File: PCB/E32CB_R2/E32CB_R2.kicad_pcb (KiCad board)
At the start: 2 copper layers, 111.3 x 90.9 mm, 89 parts, among them J1 GPIO_HEADER, J10 S, J11 Q4, J12 S, J13 Q3, J14 S, J15 Q8, J16 S, J17 Q7, J18 S, J19 Q6, J2 Power, J20 S, J21 Q5, J22 S, J3 USB_B, J4 USB +5V, J5 NEXTION, J6 I2C, J7 Q1, J8 S, J9 Q2, Q1 S8050, Q10 IRLR2905, Q2 S8050, Q3 IRLR2905, Q4 IRLR2905, Q5 IRLR2905, Q6 IRLR2905, Q7 IRLR2905, Q8 IRLR2905, Q9 IRLR2905, U1 ESP32-WROOM-32, X1 12MHz

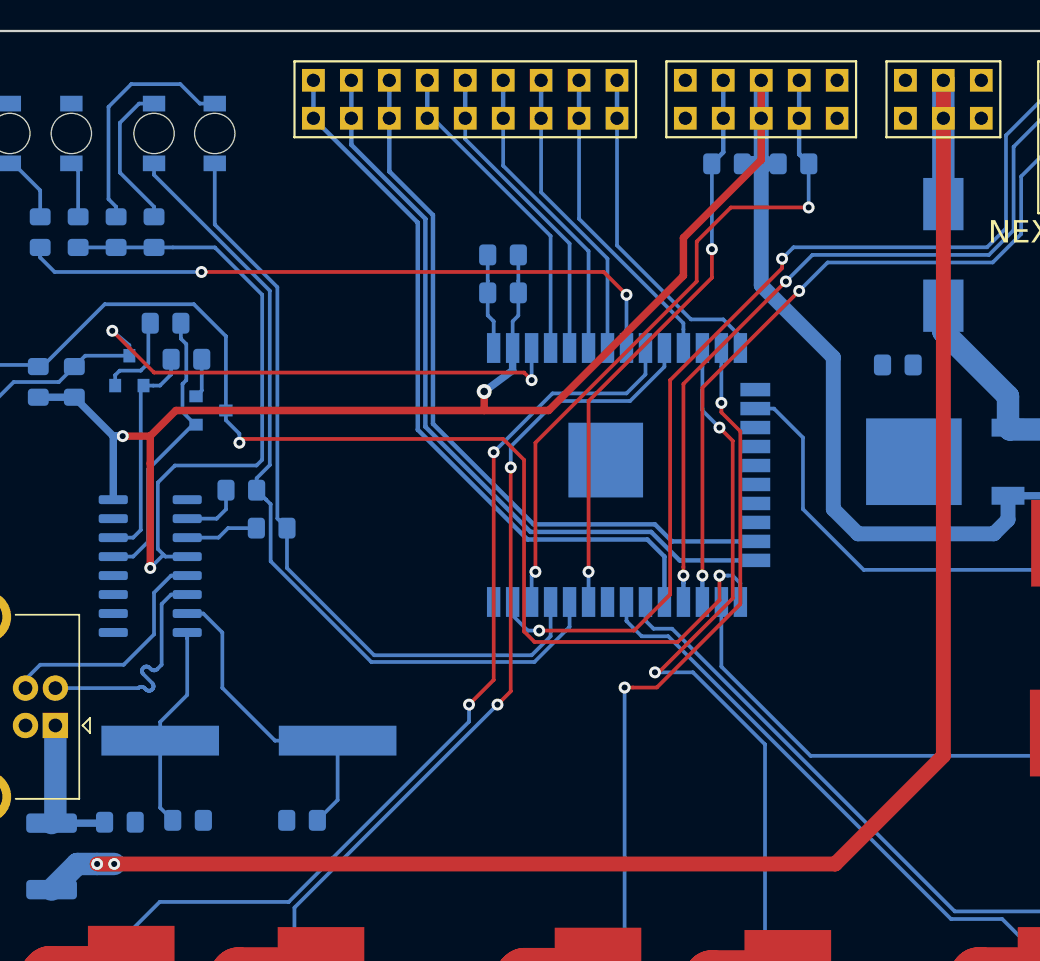
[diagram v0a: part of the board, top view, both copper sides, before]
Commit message: all conection finished
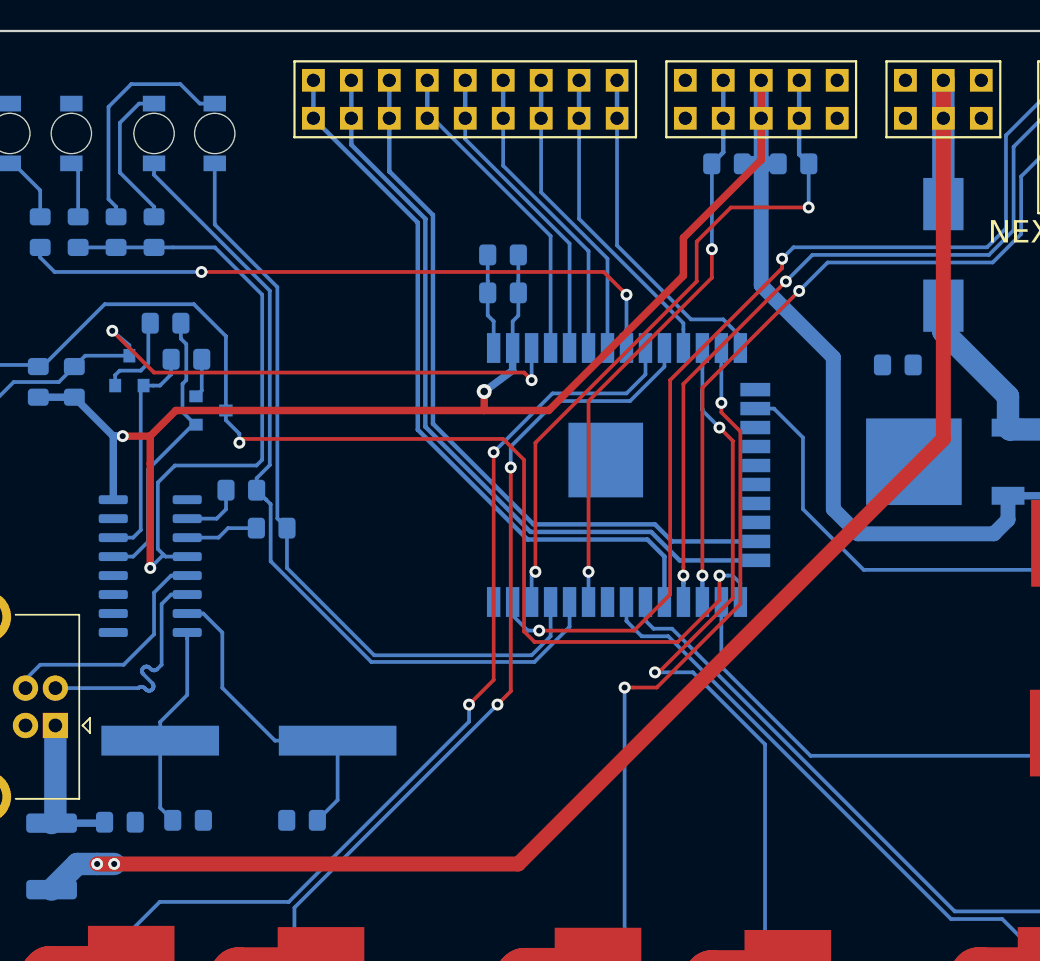
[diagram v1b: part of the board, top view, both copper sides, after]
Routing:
- net +5V: track 118.0 -> 105.6 mm
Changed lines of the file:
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@@
   (segment (start 115.062 101.727) (end 116.205 101.727) (width 1.5) (layer B.Cu) (net 83))
   (via (at 115.062 101.727) (size 0.8) (drill 0.4) (layers F.Cu B.Cu) (net 83))
-  (segment (start 115.062 101.727) (end 164.465 101.727) (width 1) (layer F.Cu) (net 83))
-  (segment (start 171.704 94.488) (end 171.704 49.276) (width 1) (layer F.Cu) (net 83))
-  (segment (start 164.465 101.727) (end 171.704 94.488) (width 1) (layer F.Cu) (net 83))
+  (segment (start 171.704 73.279) (end 171.704 49.276) (width 1) (layer F.Cu) (net 83))
+  (segment (start 115.062 101.727) (end 143.256 101.727) (width 1) (layer F.Cu) (net 83))
+  (segment (start 143.256 101.727) (end 171.704 73.279) (width 1) (layer F.Cu) (net 83))
   (segment (start 112.268 98.74) (end 112.014 98.994) (width 1.5) (layer B.Cu) (net 84))
   (segment (start 112.268 92.456) (end 112.268 98.74) (width 1.5) (layer B.Cu) (net 84))

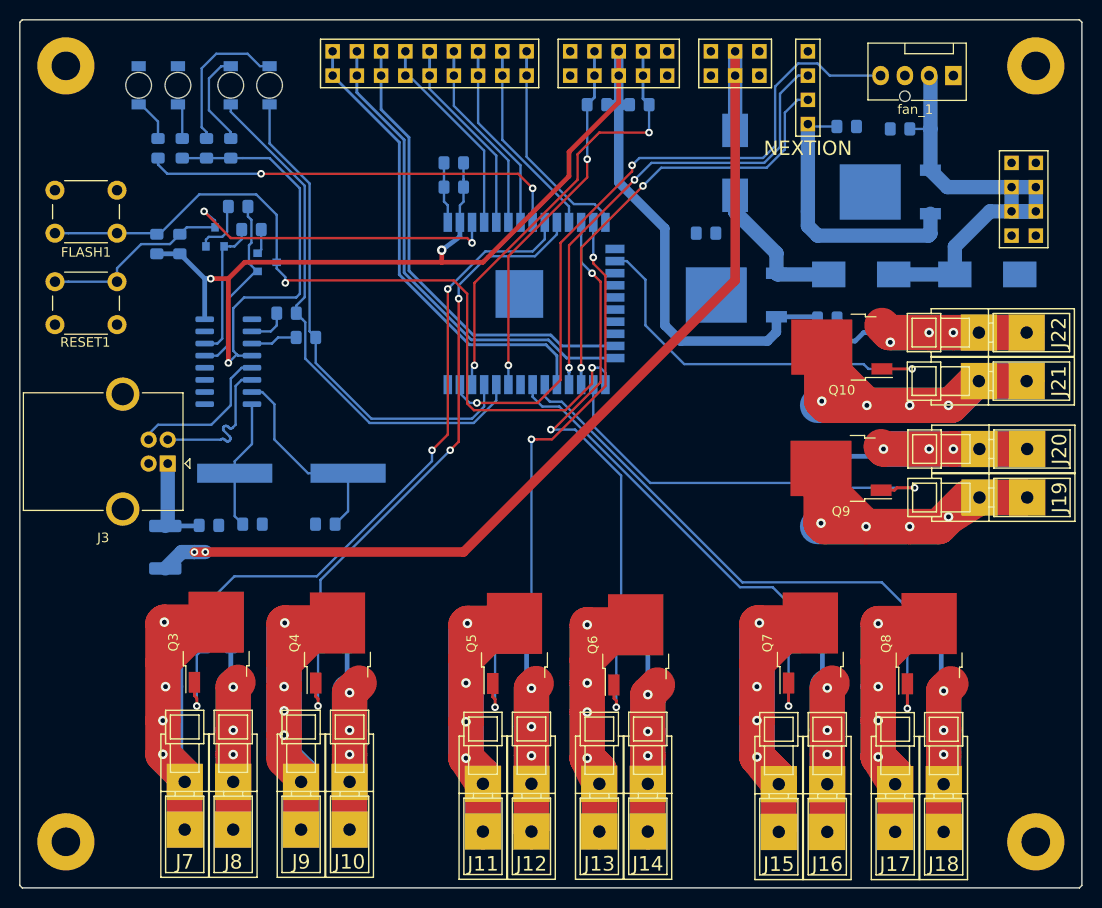
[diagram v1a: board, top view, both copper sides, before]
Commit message: filled zones
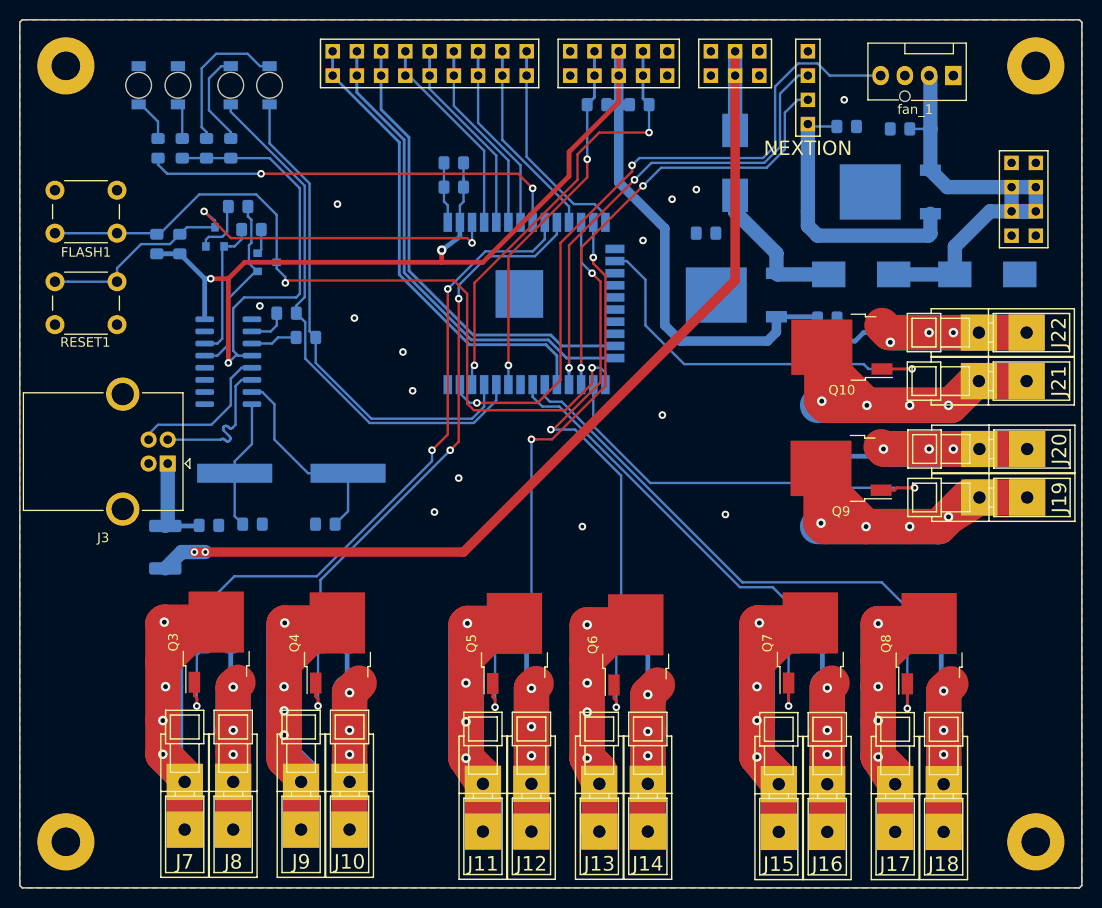
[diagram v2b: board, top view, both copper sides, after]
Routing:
- net GND: vias 0 -> 14
- added copper zone on B.Cu, net GND
- added copper zone on F.Cu, net GND
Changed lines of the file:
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@@
     (thickness 1.6)
     (drawings 8)
-    (tracks 812)
+    (tracks 826)
     (zones 0)
     (modules 89)
@@
   (segment (start 141.206 62.7) (end 141.206 60.96) (width 0.25) (layer B.Cu) (net 8))
   (segment (start 141.206 63.5) (end 141.206 62.7) (width 0.25) (layer B.Cu) (net 8))
+  (via (at 121.92 75.946) (size 0.8) (drill 0.4) (layers F.Cu B.Cu) (net 8))
+  (via (at 131.826 77.216) (size 0.8) (drill 0.4) (layers F.Cu B.Cu) (net 8))
+  (via (at 136.906 80.772) (size 0.8) (drill 0.4) (layers F.Cu B.Cu) (net 8))
+  (via (at 137.922 84.836) (size 0.8) (drill 0.4) (layers F.Cu B.Cu) (net 8))
+  (via (at 140.208 97.536) (size 0.8) (drill 0.4) (layers F.Cu B.Cu) (net 8))
+  (via (at 142.748 93.98) (size 0.8) (drill 0.4) (layers F.Cu B.Cu) (net 8))
+  (via (at 170.688 97.79) (size 0.8) (drill 0.4) (layers F.Cu B.Cu) (net 8))
+  (via (at 164.084 87.376) (size 0.8) (drill 0.4) (layers F.Cu B.Cu) (net 8))
+  (via (at 165.1 64.77) (size 0.8) (drill 0.4) (layers F.Cu B.Cu) (net 8))
+  (via (at 167.64 63.754) (size 0.8) (drill 0.4) (layers F.Cu B.Cu) (net 8))
+  (via (at 162.052 69.088) (size 0.8) (drill 0.4) (layers F.Cu B.Cu) (net 8))
+  (via (at 183.134 54.356) (size 0.8) (drill 0.4) (layers F.Cu B.Cu) (net 8))
+  (via (at 130.048 65.278) (size 0.8) (drill 0.4) (layers F.Cu B.Cu) (net 8))
+  (via (at 155.702 99.06) (size 0.8) (drill 0.4) (layers F.Cu B.Cu) (net 8))
   (segment (start 187.244 90.932) (end 187.244 90.932) (width 3.7) (layer F.Cu) (net 9))
   (segment (start 202.296 90.932) (end 194.564 90.932) (width 3.7) (layer F.Cu) (net 9))
@@
   (segment (start 115.5 98.994) (end 115.561 98.933) (width 0.5) (layer B.Cu) (net 84))
   (segment (start 112.014 98.994) (end 115.5 98.994) (width 0.5) (layer B.Cu) (net 84))
+  (zone (net 8) (net_name GND) (layer F.Cu) (hatch edge 0.508)
+    (connect_pads (clearance 0.508))
+    (min_thickness 0.25)
+    (fill yes (arc_segments 16) (thermal_gap 0.508) (thermal_bridge_width 0.508))
+    (polygon
+      (pts
+        (xy 96.774 136.652) (xy 96.774 46.228) (xy 97.028 45.974) (xy 207.772 45.974) (xy 208.026 46.228)
+        (xy 208.026 136.652) (xy 207.772 136.906) (xy 97.028 136.906)
+      )
+    )
+  )
+  (zone (net 8) (net_name GND) (layer B.Cu) (hatch edge 0.508)
+    (connect_pads (clearance 0.508))
+    (min_thickness 0.25)
+    (fill yes (arc_segments 16) (thermal_gap 0.508) (thermal_bridge_width 0.508))
+    (polygon
+      (pts
+        (xy 96.774 136.652) (xy 96.774 46.228) (xy 97.028 45.974) (xy 207.772 45.974) (xy 208.026 46.228)
+        (xy 208.026 136.652) (xy 207.772 136.906) (xy 97.028 136.906)
+      )
+    )
+  )
 )

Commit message: vias added
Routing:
- net GND: vias 14 -> 16
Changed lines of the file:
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@@
     (thickness 1.6)
     (drawings 8)
-    (tracks 826)
+    (tracks 828)
     (zones 0)
     (modules 89)
@@
   (via (at 130.048 65.278) (size 0.8) (drill 0.4) (layers F.Cu B.Cu) (net 8))
   (via (at 155.702 99.06) (size 0.8) (drill 0.4) (layers F.Cu B.Cu) (net 8))
+  (via (at 151.892 71.12) (size 0.8) (drill 0.4) (layers F.Cu B.Cu) (net 8))
+  (via (at 150.622 81.788) (size 0.8) (drill 0.4) (layers F.Cu B.Cu) (net 8))
   (segment (start 187.244 90.932) (end 187.244 90.932) (width 3.7) (layer F.Cu) (net 9))
   (segment (start 202.296 90.932) (end 194.564 90.932) (width 3.7) (layer F.Cu) (net 9))

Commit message: silk screen update
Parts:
- renumbered FLASH1 to FLASH, RESET1 to RESET
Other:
- board text added: "3V3"
- board text added: "5V"
- board text added: "GND"
- board text added: "POWER IN 12V"
- board text added: "Power"
- board text added: "RXD"
- board text added: "SCL"
- board text added: "SDA"
- board text added: "TXD"
- board text added: "USB 5V"
- board text added: "WiFi"
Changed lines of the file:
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@@
   (general
     (thickness 1.6)
-    (drawings 8)
+    (drawings 23)
     (tracks 828)
     (zones 0)
@@
     (uvia_min_drill 0.1)
     (pcb_text_width 0.3)
-    (pcb_text_size 1.5 1.5)
+    (pcb_text_size 1.3 1.3)
     (mod_edge_width 0.15)
     (mod_text_size 0.000001 0.000001)
@@
     (descr https://www.omron.com/ecb/products/pdf/en-b3f.pdf)
     (tags "tact sw push 6mm")
-    (fp_text reference FLASH1 (at 3.25 -2 180) (layer F.SilkS)
+    (fp_text reference FLASH (at -2.771 2.54 270 unlocked) (layer F.SilkS)
       (effects (font (size 1 1) (thickness 0.15)))
     )
@@
     (descr https://www.omron.com/ecb/products/pdf/en-b3f.pdf)
     (tags "tact sw push 6mm")
-    (fp_text reference RESET1 (at 3.175 6.35) (layer F.SilkS)
+    (fp_text reference RESET (at 9.271 2.032 270 unlocked) (layer F.SilkS)
       (effects (font (size 1 1) (thickness 0.15)))
     )
@@
     (descr "4-pin CPU fan Through hole pin header, e.g. for Wieson part number 2366C888-007 Molex 47053-1000, Foxconn HF27040-M1, Tyco 1470947-1 or equivalent, see http://www.formfactors.org/developer%5Cspecs%5Crev1_2_public.pdf")
     (tags "pin header 4-pin CPU fan")
-    (fp_text reference fan_1 (at 4 -3.55 180) (layer F.SilkS)
+    (fp_text reference fan_1 (at 4 -3.55 180) (layer F.SilkS) hide
       (effects (font (size 1 1) (thickness 0.15)))
     )
@@
     (descr "USB B receptacle, Horizontal, through-hole, http://www.on-shore.com/wp-content/uploads/2015/09/usb-b1hsxx.pdf")
     (tags "USB-B receptacle horizontal through-hole")
-    (fp_text reference J3 (at 6.76 -7.77 180) (layer F.SilkS)
+    (fp_text reference J3 (at 6.76 -7.77 180) (layer F.SilkS) hide
       (effects (font (size 1 1) (thickness 0.15)))
     )
@@
       (effects (font (size 1.5 1.5) (thickness 0.15)))
     )
-    (fp_text value NEXTION (at 0 6.35) (layer F.SilkS)
+    (fp_text value NEXTION (at 0 6.35) (layer F.SilkS) hide
       (effects (font (size 1.5 1.5) (thickness 0.15)))
     )
@@
     )
   )
+  (gr_text GND (at 154.432 55.118 270) (layer F.SilkS)
+    (effects (font (size 1.3 1.3) (thickness 0.3)))
+  )
+  (gr_text SDA (at 156.972 55.118 270) (layer F.SilkS)
+    (effects (font (size 1.3 1.3) (thickness 0.3)))
+  )
+  (gr_text SCL (at 162.052 55.118 270) (layer F.SilkS)
+    (effects (font (size 1.3 1.3) (thickness 0.3)))
+  )
+  (gr_text GND (at 164.592 55.118 270) (layer F.SilkS)
+    (effects (font (size 1.3 1.3) (thickness 0.3)))
+  )
+  (gr_text 3V3 (at 159.512 55.118 270) (layer F.SilkS)
+    (effects (font (size 1.3 1.3) (thickness 0.3)))
+  )
+  (gr_text WiFi (at 109.22 56.388 270) (layer F.SilkS)
+    (effects (font (size 1.3 1.3) (thickness 0.3)))
+  )
+  (gr_text Power (at 113.284 57.404 270) (layer F.SilkS)
+    (effects (font (size 1.3 1.3) (thickness 0.3)))
+  )
+  (gr_text RXD (at 118.872 56.388 270) (layer F.SilkS)
+    (effects (font (size 1.3 1.3) (thickness 0.3)))
+  )
+  (gr_text TXD (at 122.936 56.388 270) (layer F.SilkS)
+    (effects (font (size 1.3 1.3) (thickness 0.3)))
+  )
+  (gr_text "POWER IN 12V" (at 197.866 64.77 270) (layer F.SilkS)
+    (effects (font (size 1.3 1.3) (thickness 0.3)))
+  )
+  (gr_text "USB 5V" (at 171.704 54.356) (layer F.SilkS)
+    (effects (font (size 1.3 1.3) (thickness 0.3)))
+  )
+  (gr_text TXD (at 182.88 51.816) (layer F.SilkS)
+    (effects (font (size 1.3 1.3) (thickness 0.3)))
+  )
+  (gr_text 5V (at 182.118 56.896) (layer F.SilkS)
+    (effects (font (size 1.3 1.3) (thickness 0.3)))
+  )
+  (gr_text GND (at 182.88 49.276) (layer F.SilkS)
+    (effects (font (size 1.3 1.3) (thickness 0.3)))
+  )
+  (gr_text RXD (at 182.88 54.356) (layer F.SilkS)
+    (effects (font (size 1.3 1.3) (thickness 0.3)))
+  )
   (gr_line (start 207.772 136.906) (end 208.026 136.652) (layer Edge.Cuts) (width 0.15))
   (gr_line (start 97.028 136.906) (end 207.772 136.906) (layer Edge.Cuts) (width 0.15))
@@
   (via (at 167.64 63.754) (size 0.8) (drill 0.4) (layers F.Cu B.Cu) (net 8))
   (via (at 162.052 69.088) (size 0.8) (drill 0.4) (layers F.Cu B.Cu) (net 8))
-  (via (at 183.134 54.356) (size 0.8) (drill 0.4) (layers F.Cu B.Cu) (net 8))
+  (via (at 186.182 55.118) (size 0.8) (drill 0.4) (layers F.Cu B.Cu) (net 8))
   (via (at 130.048 65.278) (size 0.8) (drill 0.4) (layers F.Cu B.Cu) (net 8))
   (via (at 155.702 99.06) (size 0.8) (drill 0.4) (layers F.Cu B.Cu) (net 8))

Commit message: silk screen update
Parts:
- added REF**: ESD-Logo_13.2x12mm_SilkScreen, Symbol:ESD-Logo_13.2x12mm_SilkScreen, F.Cu at (162.8, 95.6)
- renumbered CH340G1 to CH340G, 5Vstabilizer1 to L7805, 3V3stabilizer1 to LF33
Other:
- board text added: "ESP32-WROOM32"
- board text added: "GPI34"
- board text added: "GPI35"
- board text added: "GPI36"
- board text added: "GPI39"
- board text added: "GPIO12"
- board text added: "GPIO15"
- board text added: "GPIO2"
- board text added: "GPIO26"
- board text added: "GPIO5"
- board text added: "POWER 12V"
- board text removed: "POWER IN 12V"

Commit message: vias added
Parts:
- added REF**: RoHS-Logo_6mm_SilkScreen, Symbol:RoHS-Logo_6mm_SilkScreen, B.Cu at (103.9, 113.4)
- REF**: moved to B.Cu
- moved REF** 14.0 mm to (148.8, 96.8), turned to 180 degrees
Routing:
- net GND: vias 16 -> 18

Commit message: track update
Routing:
- net Net-(3V3stabilizer1-Pad1): track 15.5 -> 18.9 mm
- net +3V3: track 181.2 -> 180.3 mm
- net /RXD: track 56.0 -> 55.5 mm
- removed copper zone on B.Cu, net GND

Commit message: refill zones
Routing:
- added copper zone on B.Cu, net GND
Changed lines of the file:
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@@
   )
   (setup
-    (last_trace_width 0.3)
+    (last_trace_width 1)
     (user_trace_width 0.3)
     (user_trace_width 0.5)
@@
     (user_trace_width 3.7)
     (trace_clearance 0.2)
-    (zone_clearance 0.508)
+    (zone_clearance 0.3)
     (zone_45_only no)
     (trace_min 0.1)
@@
   (segment (start 112.014 98.994) (end 115.5 98.994) (width 0.5) (layer B.Cu) (net 84))
   (zone (net 8) (net_name GND) (layer F.Cu) (hatch edge 0.508)
-    (connect_pads (clearance 0.508))
+    (connect_pads (clearance 0.3))
+    (min_thickness 0.25)
+    (fill yes (arc_segments 16) (thermal_gap 0.508) (thermal_bridge_width 0.508))
+    (polygon
+      (pts
+        (xy 96.774 136.652) (xy 96.774 46.228) (xy 97.028 45.974) (xy 207.772 45.974) (xy 208.026 46.228)
+        (xy 208.026 136.652) (xy 207.772 136.906) (xy 97.028 136.906)
+      )
+    )
+  )
+  (zone (net 8) (net_name GND) (layer B.Cu) (hatch edge 0.508)
+    (connect_pads (clearance 0.3))
     (min_thickness 0.25)
     (fill yes (arc_segments 16) (thermal_gap 0.508) (thermal_bridge_width 0.508))
